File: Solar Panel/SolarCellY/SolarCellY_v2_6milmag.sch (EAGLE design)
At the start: 23 parts

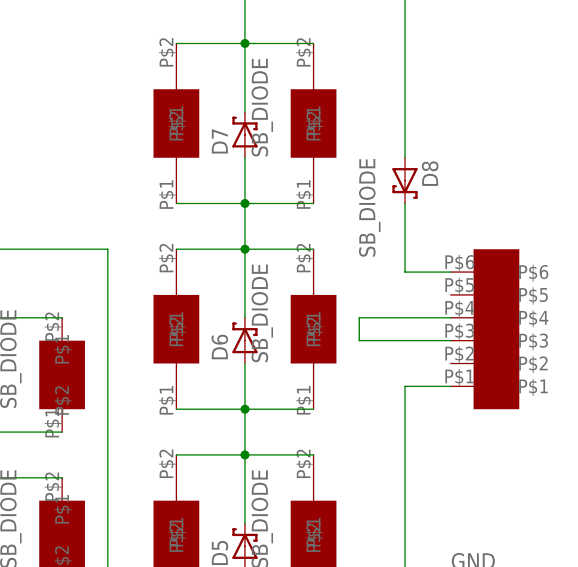
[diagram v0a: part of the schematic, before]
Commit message: Changed connector config and DRC stuff for Y panel
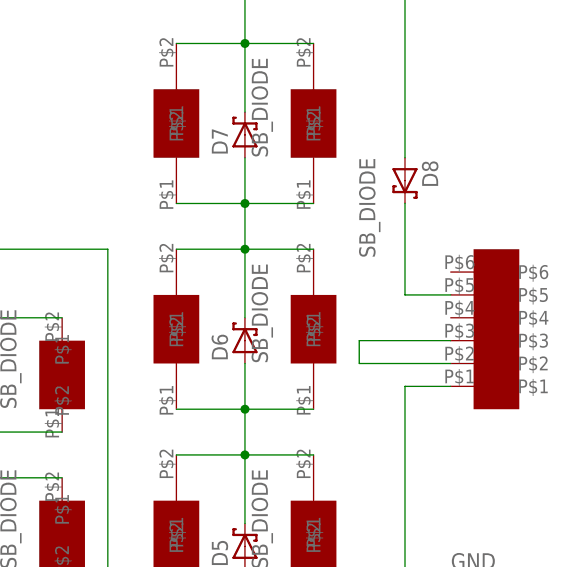
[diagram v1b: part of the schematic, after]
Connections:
- net N$1: now also U$1.P$2; no longer U$1.P$4
- net N$14: now also U$1.P$5; no longer U$1.P$6
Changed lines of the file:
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@@
 <setting verticaltext="up"/>
 </settings>
-<grid distance="0.1" unitdist="inch" unit="inch" style="lines" multiple="1" display="no" altdistance="0.01" altunitdist="inch" altunit="inch"/>
+<grid distance="1" unitdist="mil" unit="mil" style="lines" multiple="1" display="yes" altdistance="0.01" altunitdist="inch" altunit="inch"/>
 <layers>
 <layer number="1" name="Top" color="4" fill="1" visible="no" active="no"/>
@@
 <net name="N$1" class="0">
 <segment>
-<pinref part="U$1" gate="G$1" pin="P$4"/>
-<wire x1="114.3" y1="53.34" x2="104.14" y2="53.34" width="0.1524" layer="91"/>
-<wire x1="104.14" y1="53.34" x2="104.14" y2="50.8" width="0.1524" layer="91"/>
 <pinref part="U$1" gate="G$1" pin="P$3"/>
 <wire x1="104.14" y1="50.8" x2="114.3" y2="50.8" width="0.1524" layer="91"/>
+<pinref part="U$1" gate="G$1" pin="P$2"/>
+<wire x1="104.14" y1="50.8" x2="104.14" y2="48.26" width="0.1524" layer="91"/>
+<wire x1="104.14" y1="48.26" x2="114.3" y2="48.26" width="0.1524" layer="91"/>
 </segment>
 </net>
@@
 <segment>
 <pinref part="D8" gate="G$1" pin="NEG"/>
-<wire x1="109.22" y1="58.42" x2="109.22" y2="66.04" width="0.1524" layer="91"/>
-<pinref part="U$1" gate="G$1" pin="P$6"/>
-<wire x1="109.22" y1="58.42" x2="114.3" y2="58.42" width="0.1524" layer="91"/>
-</segment>
-</net>
+<wire x1="109.22" y1="55.88" x2="109.22" y2="66.04" width="0.1524" layer="91"/>
+<pinref part="U$1" gate="G$1" pin="P$5"/>
+<wire x1="109.22" y1="55.88" x2="114.3" y2="55.88" width="0.1524" layer="91"/>
+</segment>
+</net>
